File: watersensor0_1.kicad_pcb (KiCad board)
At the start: 2 copper layers, 25.4 x 133.4 mm, 18 parts, among them U1 DIP-8_W7.62mm, U2 DIP-8_W7.62mm

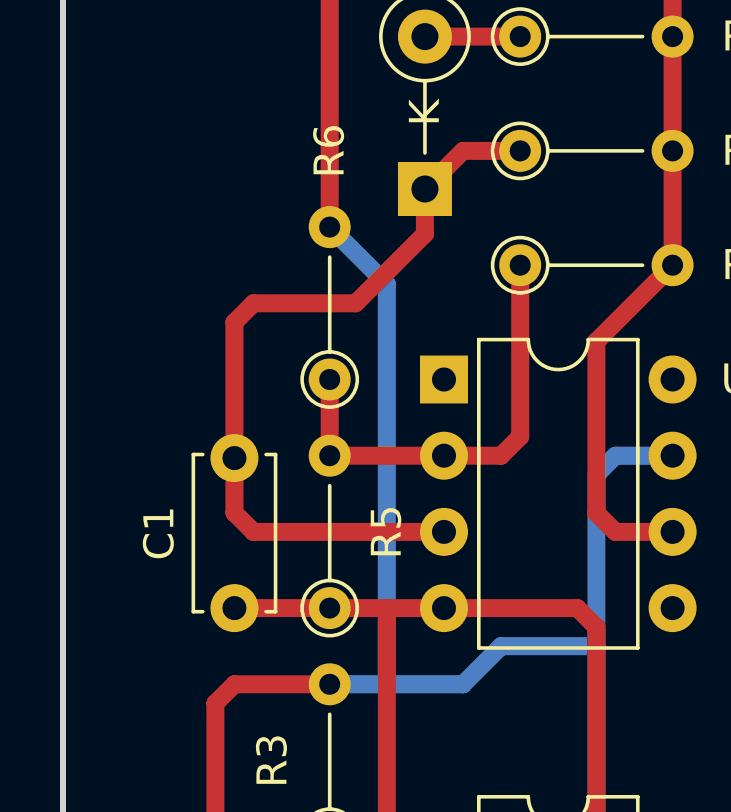
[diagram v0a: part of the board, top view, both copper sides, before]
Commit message: added part placement guide
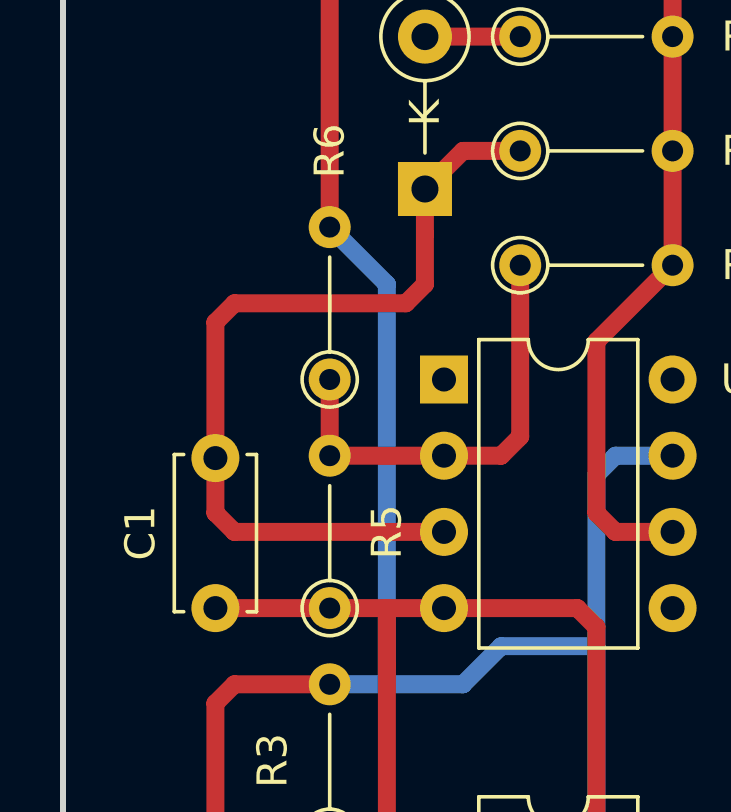
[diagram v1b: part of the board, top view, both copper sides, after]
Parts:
- moved C1 0.64 mm to (119.4, 90.2)
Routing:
- net (no net): track 468.6 -> 470.8 mm
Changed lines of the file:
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@@
     (thickness 1.6)
     (drawings 40)
-    (tracks 94)
+    (tracks 95)
     (zones 0)
     (modules 18)
@@
   )
   (module Capacitor_THT:C_Disc_D5.0mm_W2.5mm_P5.00mm (layer F.Cu)
-    (at 120.015 90.17 90)
+    (at 119.38 90.17 90)
     (descr "C, Disc series, Radial, pin pitch=5.00mm, , diameter*width=5*2.5mm^2, Capacitor, http://cdn-reichelt.de/documents/datenblatt/B300/DS_KERKO_TC.pdf")
     (tags "C Disc series Radial pin pitch 5.00mm  diameter 5mm width 2.5mm Capacitor")
@@
   (segment (start 125.095 92.075) (end 125.095 90.17) (width 0.6) (layer F.Cu) (net 0))
   (segment (start 120.015 90.17) (end 123.19 90.17) (width 0.6) (layer F.Cu) (net 0))
-  (segment (start 127 87.63) (end 120.65 87.63) (width 0.6) (layer F.Cu) (net 0))
-  (segment (start 120.015 86.995) (end 120.015 85.17) (width 0.6) (layer F.Cu) (net 0))
-  (segment (start 120.65 87.63) (end 120.015 86.995) (width 0.6) (layer F.Cu) (net 0))
-  (segment (start 120.65 80.01) (end 120.015 80.645) (width 0.6) (layer F.Cu) (net 0))
-  (segment (start 120.015 80.645) (end 120.015 85.17) (width 0.6) (layer F.Cu) (net 0))
-  (segment (start 124.055 80.01) (end 120.65 80.01) (width 0.6) (layer F.Cu) (net 0))
-  (segment (start 126.365 76.2) (end 126.365 77.7) (width 0.6) (layer F.Cu) (net 0))
-  (segment (start 126.365 77.7) (end 124.055 80.01) (width 0.6) (layer F.Cu) (net 0))
   (segment (start 134.62 67.31) (end 134.62 71.12) (width 0.6) (layer F.Cu) (net 0))
   (segment (start 127 114.3) (end 127 113.03) (width 0.6) (layer B.Cu) (net 0))
@@
   (segment (start 119.38 128.27) (end 127 135.89) (width 0.6) (layer F.Cu) (net 0))
   (segment (start 127 135.89) (end 127 143.51) (width 0.6) (layer F.Cu) (net 0))
+  (segment (start 119.38 86.995) (end 119.38 85.17) (width 0.6) (layer F.Cu) (net 0))
+  (segment (start 127 87.63) (end 120.015 87.63) (width 0.6) (layer F.Cu) (net 0))
+  (segment (start 120.015 87.63) (end 119.38 86.995) (width 0.6) (layer F.Cu) (net 0))
+  (segment (start 126.365 77.7) (end 126.365 76.2) (width 0.6) (layer F.Cu) (net 0))
+  (segment (start 126.365 79.375) (end 126.365 77.7) (width 0.6) (layer F.Cu) (net 0))
+  (segment (start 125.73 80.01) (end 126.365 79.375) (width 0.6) (layer F.Cu) (net 0))
+  (segment (start 120.015 80.01) (end 125.73 80.01) (width 0.6) (layer F.Cu) (net 0))
+  (segment (start 119.38 85.17) (end 119.38 80.645) (width 0.6) (layer F.Cu) (net 0))
+  (segment (start 119.38 80.645) (end 120.015 80.01) (width 0.6) (layer F.Cu) (net 0))
 )

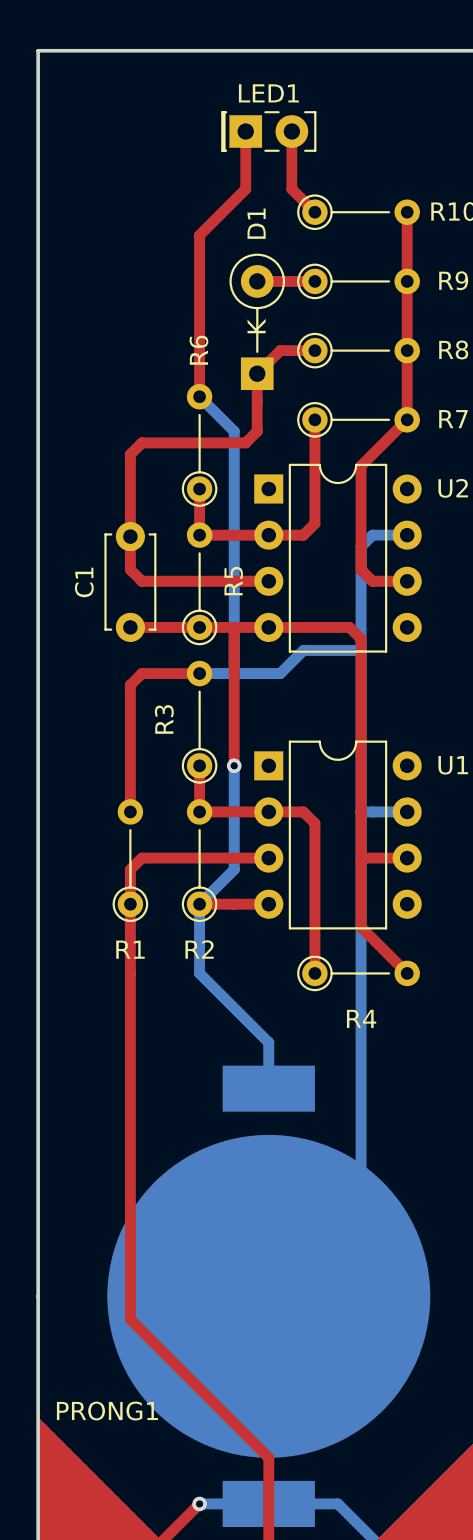
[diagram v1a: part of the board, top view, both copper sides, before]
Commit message: added my name and the OSHW logo
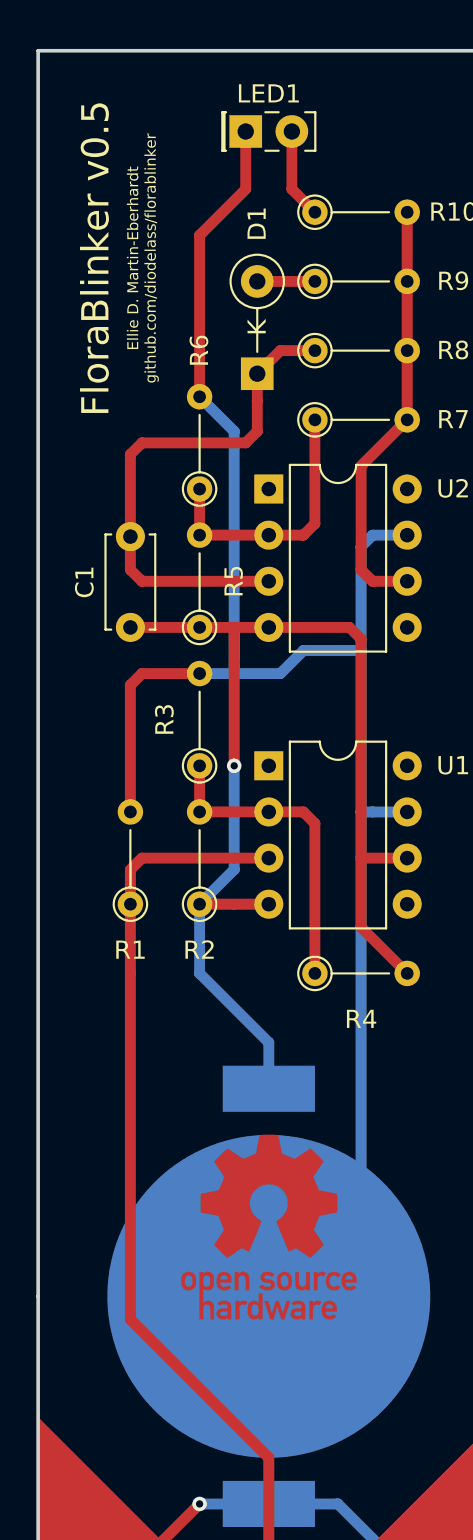
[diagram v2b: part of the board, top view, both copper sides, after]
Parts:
- added G*** (x2): LOGO, LOGO, F.Cu at (127.0, 123.2)
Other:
- board text added: "Ellie D. Martin-Eberhardt github.com/diodelass/florablinker"
- board text added: "FloraBlinker v0.5"

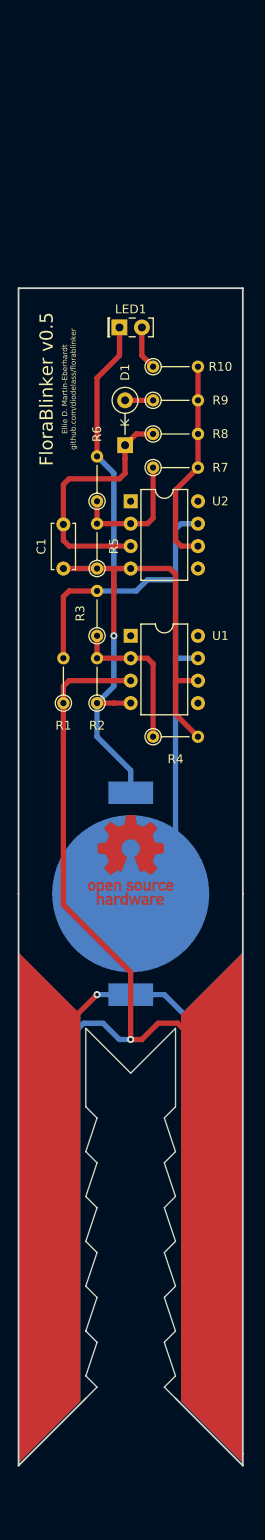
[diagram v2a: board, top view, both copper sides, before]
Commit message: fixed wiring bugs
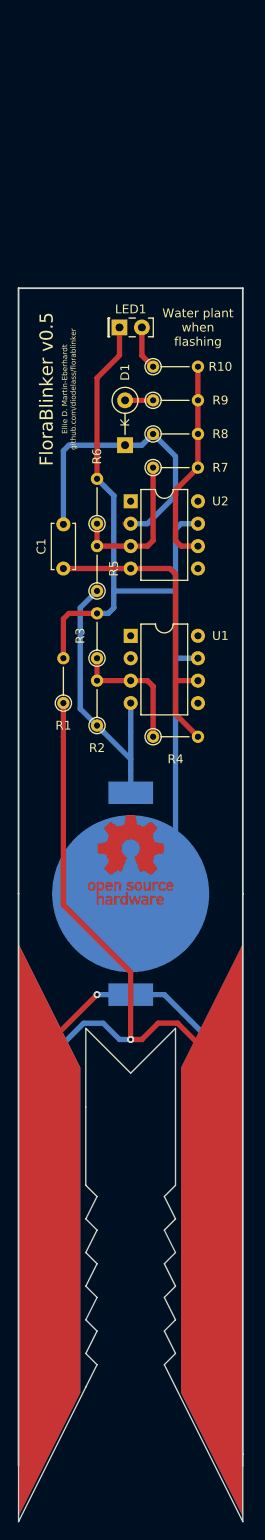
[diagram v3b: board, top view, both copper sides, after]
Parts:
- removed PRONG1, PRONG2: WaterSensorProngs, WaterSensorProngs
- added REF**: WaterSensorProngs, WaterSensorProngs, B.Cu at (139.7, 165.1)
- added REF**: WaterSensorProngs, WaterSensorProngs, F.Cu at (139.7, 165.1)
- moved R2 2.54 mm to (123.2, 108.0)
- moved R6 2.54 mm to (123.2, 85.1)
- moved R3 2.54 mm to (123.2, 100.3)
- moved R5 2.54 mm to (123.2, 92.7)
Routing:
- net (no net): track 470.8 -> 466.0 mm, vias 3 -> 2
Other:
- board size 25.4 x 133.4 mm -> 25.4 x 139.7 mm
- board text added: "Water plant when flashing"

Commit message: adjusted track routing
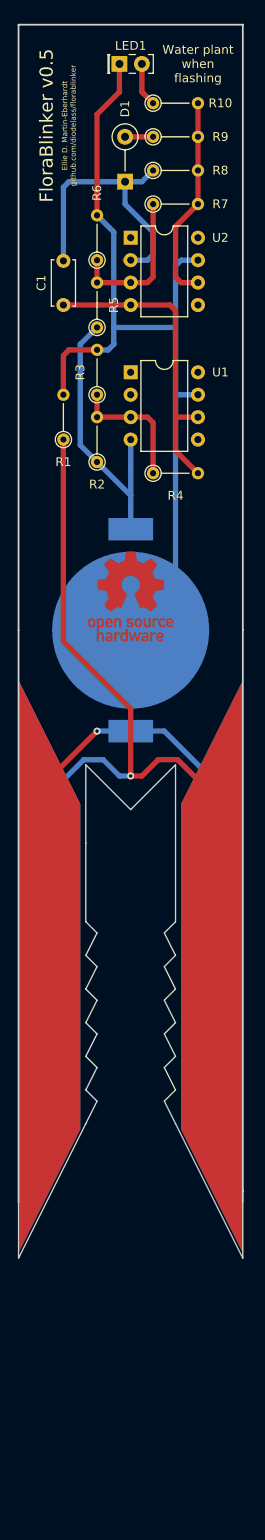
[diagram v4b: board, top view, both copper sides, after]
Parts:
- moved U1 29.8 mm to (127.0, 67.9)
- moved D1 29.8 mm to (126.4, 46.4)
- moved R6 29.8 mm to (123.2, 55.2)
- moved R8 29.8 mm to (129.5, 45.1)
- moved R9 29.8 mm to (129.5, 41.3)
- moved BAT1 29.8 mm to (127.0, 97.2)
- moved C1 29.8 mm to (119.4, 60.3)
- moved G*** 29.8 mm to (127.0, 93.3) (x2)
- moved LED1 29.8 mm to (125.7, 33.0)
- moved R1 29.8 mm to (119.4, 75.6)
- moved R10 29.8 mm to (129.5, 37.5)
- moved R2 29.8 mm to (123.2, 78.1)
- moved R3 29.8 mm to (123.2, 70.5)
- moved R4 29.8 mm to (129.5, 79.4)
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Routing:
- net (no net): track 466.0 -> 463.9 mm

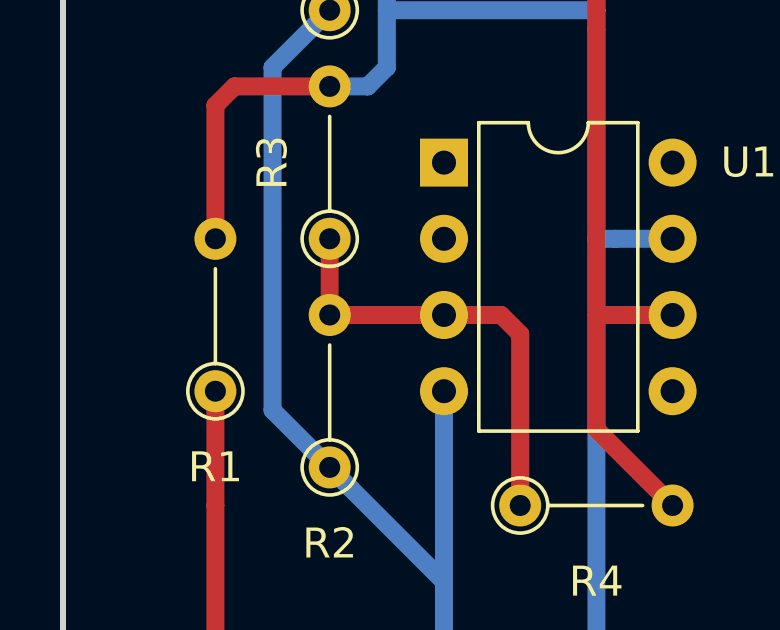
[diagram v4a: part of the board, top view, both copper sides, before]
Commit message: fixed wiring error
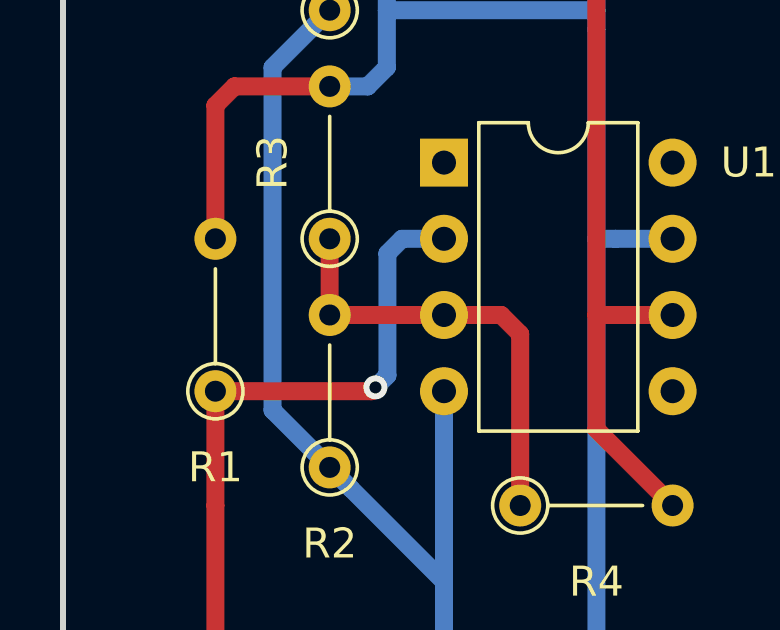
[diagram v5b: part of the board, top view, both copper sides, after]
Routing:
- net (no net): track 463.9 -> 476.0 mm, vias 2 -> 3
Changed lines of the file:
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@@
-(kicad_pcb (version 20171130) (host pcbnew 5.0.0+dfsg1-2)
+(kicad_pcb (version 20171130) (host pcbnew 5.0.2+dfsg1-1)
   (general
     (thickness 1.6)
     (drawings 46)
-    (tracks 93)
+    (tracks 100)
     (zones 0)
     (modules 20)
@@
     (pad_drill 0.762)
     (pad_to_mask_clearance 0.2)
+    (solder_mask_min_width 0.25)
     (aux_axis_origin 0 0)
-    (visible_elements FFFFFF7F)
+    (visible_elements 7FFFFFFF)
     (pcbplotparams
       (layerselection 0x010fc_ffffffff)
@@
   (segment (start 119.38 46.99) (end 119.38 55.325) (width 0.6) (layer B.Cu) (net 0))
   (segment (start 126.365 46.355) (end 120.015 46.355) (width 0.6) (layer B.Cu) (net 0))
+  (via (at 124.714 75.438) (size 0.8) (drill 0.4) (layers F.Cu B.Cu) (net 0))
+  (segment (start 119.38 75.565) (end 124.587 75.565) (width 0.6) (layer F.Cu) (net 0))
+  (segment (start 124.587 75.565) (end 124.714 75.438) (width 0.6) (layer F.Cu) (net 0))
+  (segment (start 125.113999 75.038001) (end 125.113999 70.974001) (width 0.6) (layer B.Cu) (net 0))
+  (segment (start 124.714 75.438) (end 125.113999 75.038001) (width 0.6) (layer B.Cu) (net 0))
+  (segment (start 125.603 70.485) (end 127 70.485) (width 0.6) (layer B.Cu) (net 0))
+  (segment (start 125.113999 70.974001) (end 125.603 70.485) (width 0.6) (layer B.Cu) (net 0))
 )
